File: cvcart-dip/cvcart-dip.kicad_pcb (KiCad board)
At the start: 2 copper layers, 6 parts, among them CON101 CV-EDGE, U101 W27C512

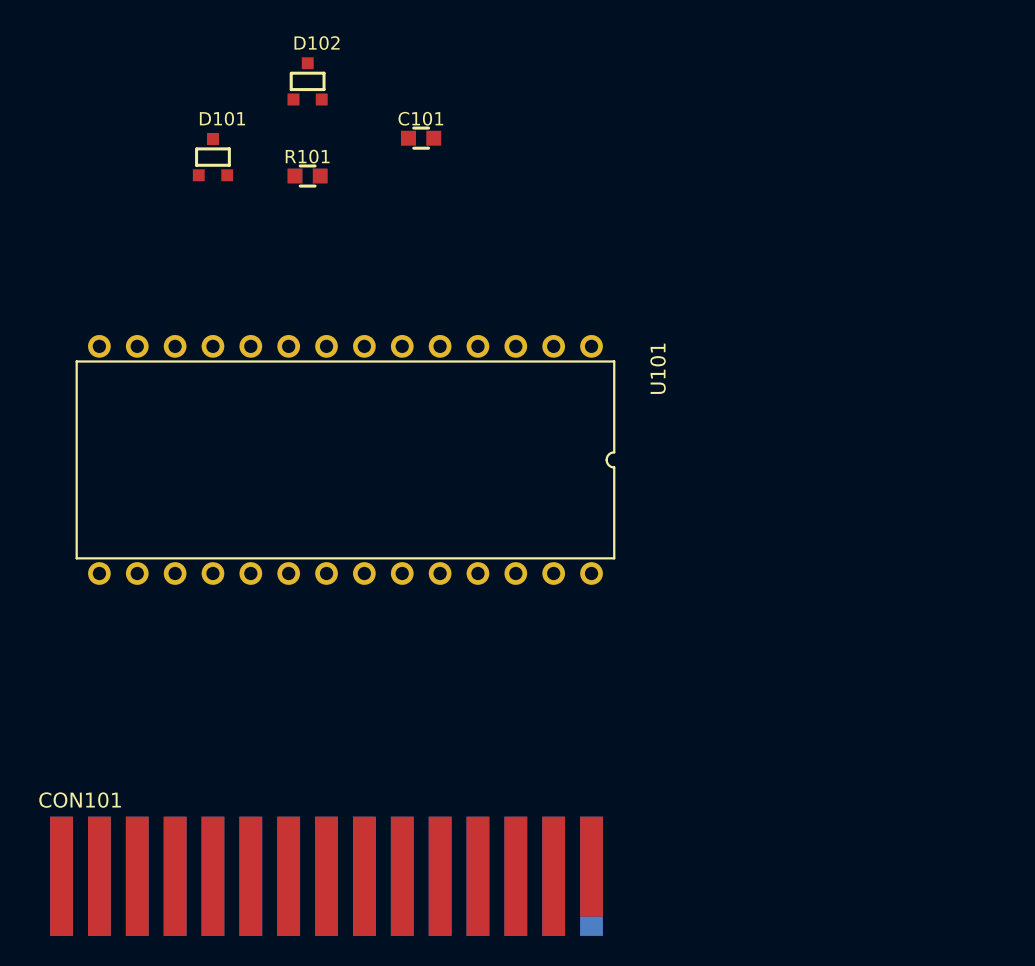
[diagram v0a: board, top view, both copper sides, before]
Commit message: routing traces
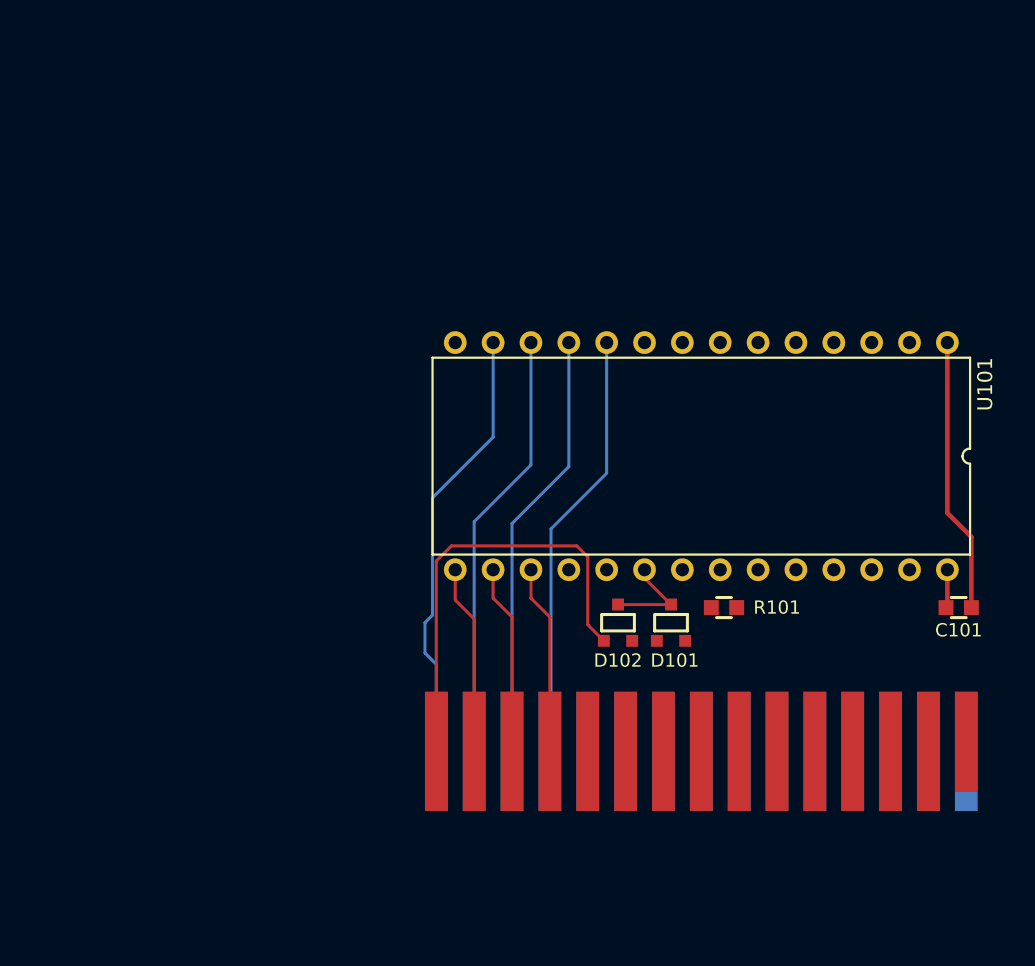
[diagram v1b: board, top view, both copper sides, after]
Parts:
- moved C101 47.9 mm to (166.9, 110.2)
- moved D101 43.8 mm to (147.6, 111.3)
- moved D102 41.9 mm to (144.0, 111.3)
- moved R101 40.2 mm to (151.1, 110.2), turned to 180 degrees
- moved CON101 26.5 mm to (131.8, 119.9)
- moved U101 23.9 mm to (166.1, 92.5)
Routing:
- net /~C000: track 0.00 -> 29.7 mm
- net /D2: track 0.00 -> 29.6 mm
- net /D0: track 0.00 -> 29.0 mm
- net /A0: track 0.00 -> 29.0 mm
- net /D1: track 0.00 -> 29.0 mm
- net GND: track 0.00 -> 18.4 mm
- net /D5: track 0.00 -> 12.7 mm
- net /D4: track 0.00 -> 12.7 mm
- net /D3: track 0.00 -> 12.7 mm
- net Net-(D101-Pad3): track 0.00 -> 6.63 mm
- net +5V: track 0.00 -> 2.58 mm
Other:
- net class Default: clearance 0.2 -> 0.1778; trace_width 0.25 -> 0.2032; via_dia 0.6 -> 0.6096; via_drill 0.4 -> 0.3048
- net class Power added: clearance 0.1778, trace_width 0.3048, via_dia 0.6096, via_drill 0.3048
- rule trace_clearance: 0.2 -> 0.1778
- rule trace_min: 0.2 -> 0.1778
- rule via_min_size: 0.4 -> 0.3048

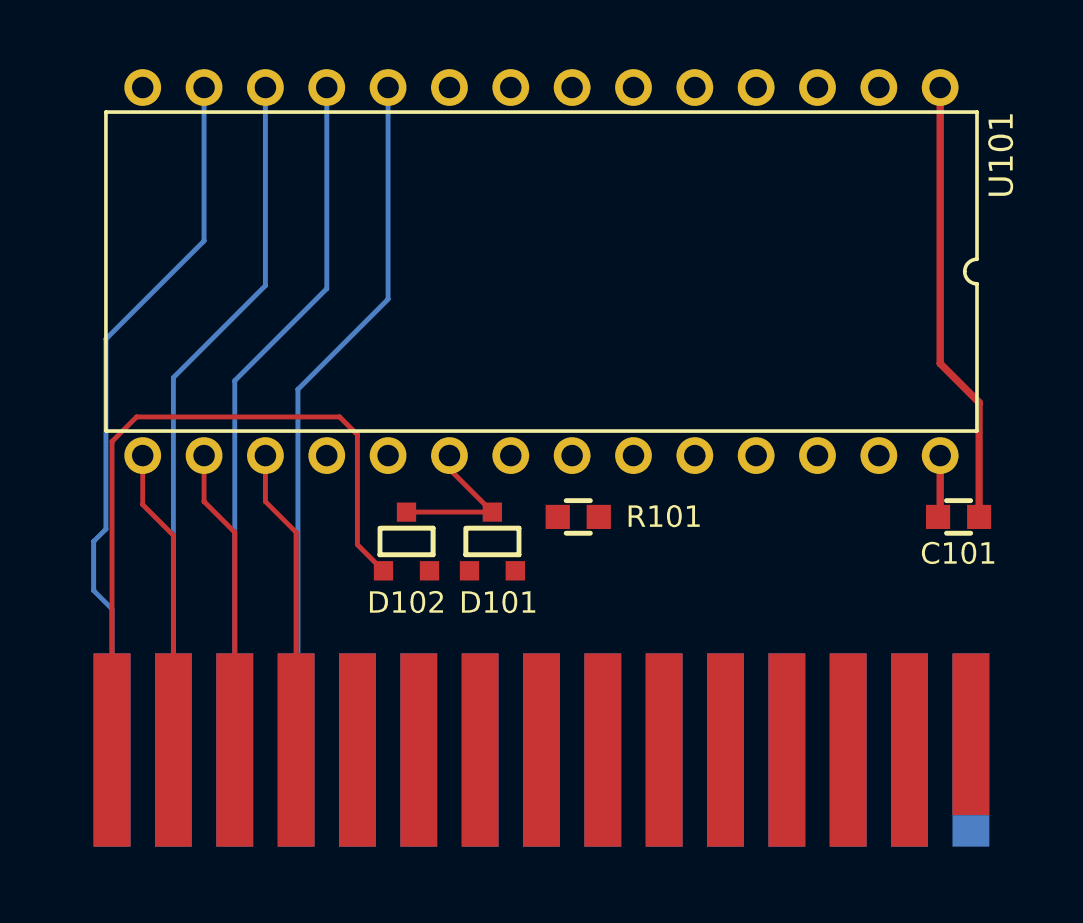
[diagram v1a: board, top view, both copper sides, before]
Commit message: layout work, missing ground plane
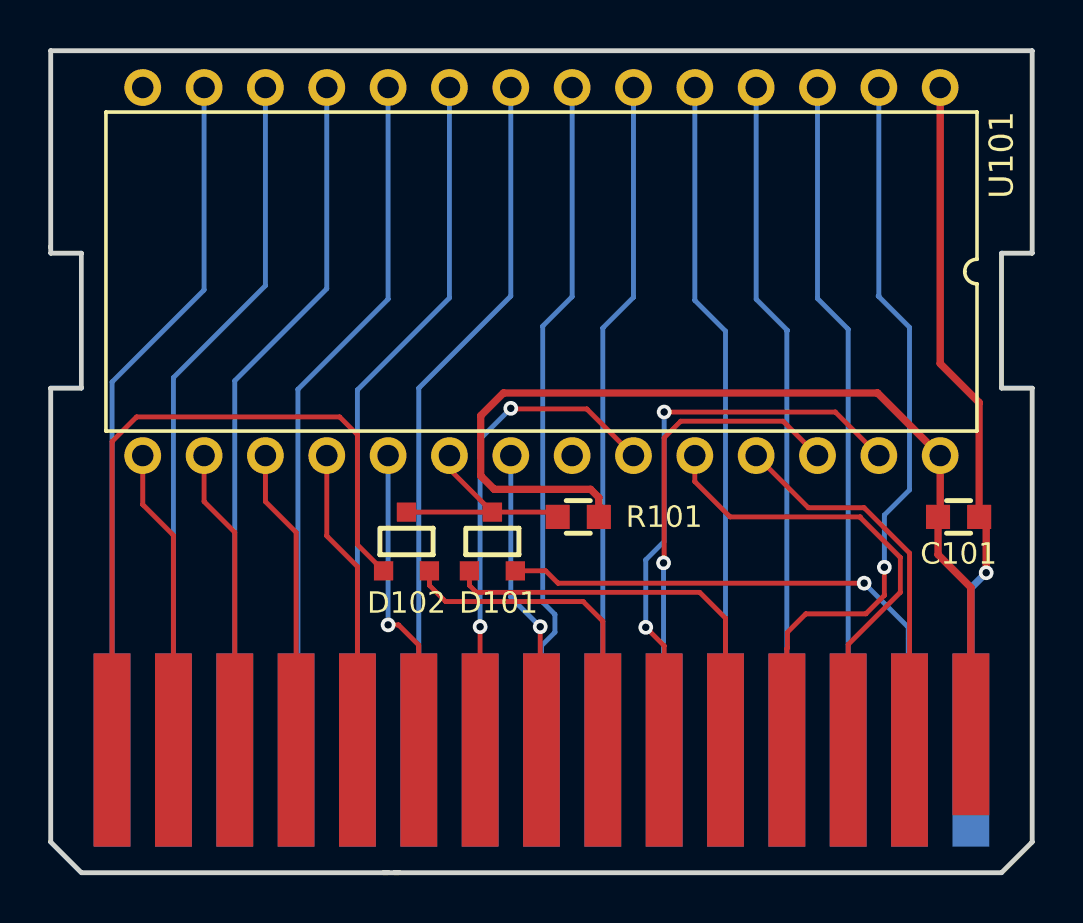
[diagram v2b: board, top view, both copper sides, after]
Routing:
- net +5V: track 2.58 -> 41.2 mm
- net /A12: track 0.00 -> 31.5 mm, vias 0 -> 1
- net /A2: track 0.00 -> 29.0 mm
- net /A1: track 0.00 -> 29.0 mm
- net /A3: track 0.00 -> 28.4 mm
- net /A6: track 0.00 -> 28.0 mm
- net /A7: track 0.00 -> 28.0 mm
- net /A5: track 0.00 -> 28.0 mm
- net /A4: track 0.00 -> 28.0 mm
- net /A14: track 0.00 -> 24.3 mm, vias 0 -> 2
- net /~E000: track 0.00 -> 22.3 mm, vias 0 -> 1
- net /A11: track 0.00 -> 21.3 mm, vias 0 -> 2
- net /A13: track 0.00 -> 20.2 mm, vias 0 -> 1
- net /A9: track 0.00 -> 19.8 mm
- net /~A000: track 0.00 -> 17.2 mm
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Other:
- board outline added: 40.6 x 34 mm

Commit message: added ground pours and keepouts
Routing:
- net GND: track 28.5 -> 33.1 mm, vias 1 -> 2
- added copper zone on B.Cu, net GND
- added copper zone on F.Cu, net GND
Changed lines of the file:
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@@
   (general
     (links 37)
-    (no_connects 23)
+    (no_connects 2)
     (area 115.086001 82.136 187.729715 125.068001)
     (thickness 1.6)
     (drawings 22)
-    (tracks 165)
+    (tracks 167)
     (zones 0)
     (modules 6)
@@
     (last_trace_width 0.2032)
     (trace_clearance 0.1778)
-    (zone_clearance 0.508)
-    (zone_45_only no)
+    (zone_clearance 0.381)
+    (zone_45_only yes)
     (trace_min 0.1778)
     (segment_width 0.2)
@@
       (outputformat 1)
       (mirror false)
-      (drillshape 1)
+      (drillshape 0)
       (scaleselection 1)
       (outputdirectory ""))
@@
       (effects (font (size 1 1) (thickness 0.15)))
     )
-    (fp_text value W27C512 (at 2.54 35.56 270) (layer F.Fab)
+    (fp_text value W27C512 (at 2.6162 -2.5908 270) (layer F.Fab)
       (effects (font (size 1 1) (thickness 0.15)))
     )
@@
   (segment (start 139.446 110.871) (end 139.446 119.888) (width 0.2032) (layer F.Cu) (net 2))
   (segment (start 138.176 109.601) (end 139.446 110.871) (width 0.2032) (layer F.Cu) (net 2))
+  (segment (start 150.876 107.696) (end 150.876 103.0732) (width 0.3048) (layer B.Cu) (net 3))
+  (via (at 150.876 103.0732) (size 0.6096) (drill 0.3048) (layers F.Cu B.Cu) (net 3))
   (segment (start 168.021 112.5474) (end 168.021 110.529) (width 0.3048) (layer F.Cu) (net 3))
   (segment (start 168.021 110.529) (end 167.728 110.236) (width 0.3048) (layer F.Cu) (net 3))
@@
   (segment (start 145.796 108.258) (end 147.574 110.036) (width 0.2032) (layer F.Cu) (net 31))
   (segment (start 144.018 110.036) (end 147.574 110.036) (width 0.2032) (layer F.Cu) (net 31) (status 10))
+  (zone (net 0) (net_name "") (layer F.Cu) (hatch full 0.508)
+    (connect_pads (clearance 0.508))
+    (min_thickness 0.254)
+    (keepout (tracks allowed) (vias allowed) (copperpour not_allowed))
+    (fill (arc_segments 16) (thermal_gap 0.508) (thermal_bridge_width 0.508))
+    (polygon
+      (pts
+        (xy 129.286 115.57) (xy 129.286 124.968) (xy 169.9514 124.968) (xy 169.926 115.57)
+      )
+    )
+  )
+  (zone (net 3) (net_name GND) (layer F.Cu) (hatch full 0.508)
+    (connect_pads (clearance 0.381))
+    (min_thickness 0.2032)
+    (fill yes (arc_segments 16) (thermal_gap 0.3048) (thermal_bridge_width 0.254))
+    (polygon
+      (pts
+        (xy 129.286 90.932) (xy 129.286 124.968) (xy 169.926 124.968) (xy 169.926 90.932)
+      )
+    )
+  )
+  (zone (net 3) (net_name GND) (layer B.Cu) (hatch full 0.508)
+    (connect_pads (clearance 0.381))
+    (min_thickness 0.2032)
+    (fill yes (arc_segments 16) (thermal_gap 0.3048) (thermal_bridge_width 0.254))
+    (polygon
+      (pts
+        (xy 129.286 90.932) (xy 129.286 124.968) (xy 169.926 124.968) (xy 169.9006 90.932)
+      )
+    )
+  )
+  (zone (net 0) (net_name "") (layer B.Cu) (hatch full 0.508)
+    (connect_pads (clearance 0.508))
+    (min_thickness 0.254)
+    (keepout (tracks allowed) (vias allowed) (copperpour not_allowed))
+    (fill (arc_segments 16) (thermal_gap 0.508) (thermal_bridge_width 0.508))
+    (polygon
+      (pts
+        (xy 129.286 115.57) (xy 129.286 124.968) (xy 169.926 124.968) (xy 169.926 115.57)
+      )
+    )
+  )
 )

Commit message: fully licensed as CERN OHL v.1.2
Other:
- board text added: "cvcart-dip_1.0 René Richard Licensed under CERN OHL v.1.2 https://github.com/db-electronics/cvcarts-kicad"
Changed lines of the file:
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@@
-(kicad_pcb (version 4) (host pcbnew 4.0.5-e0-6337~49~ubuntu16.04.1)
+(kicad_pcb (version 4) (host pcbnew 4.0.7-e2-6376~58~ubuntu16.04.1)
   (general
     (links 37)
-    (no_connects 2)
+    (no_connects 0)
     (area 115.086001 82.136 187.729715 125.068001)
     (thickness 1.6)
-    (drawings 22)
+    (drawings 23)
     (tracks 167)
     (zones 0)
@@
   )
   (page A4)
+  (title_block
+    (title "Colecovision DIP Cartridge")
+    (date 2017-10-16)
+    (rev 1.0)
+    (company "db Electronics")
+    (comment 1 "copyright: René Richard")
+    (comment 2 https://github.com/db-electronics/cvcarts-kicad)
+    (comment 3 http://ohwr.org/cernohl)
+    (comment 4 "Licensed under CERN OHL v.1.2”")
+  )
   (layers
     (0 F.Cu signal)
@@
     (descr SOT23)
     (attr smd)
-    (fp_text reference D101 (at 0.254 2.54) (layer F.SilkS)
+    (fp_text reference D101 (at 3.7084 1.016) (layer F.SilkS)
       (effects (font (size 0.889 0.889) (thickness 0.2032)))
     )
@@
     (descr SOT23)
     (attr smd)
-    (fp_text reference D102 (at 0 2.54) (layer F.SilkS)
+    (fp_text reference D102 (at -2.667 -1.2954) (layer F.SilkS)
       (effects (font (size 0.889 0.889) (thickness 0.2032)))
     )
@@
     )
   )
+  (gr_text "cvcart-dip_1.0\nRené Richard\nLicensed under CERN OHL v.1.2\nhttps://github.com/db-electronics/cvcarts-kicad" (at 167.005 98.3742) (layer B.SilkS)
+    (effects (font (size 0.889 0.889) (thickness 0.2032)) (justify left mirror))
+  )
   (gr_line (start 143.0782 124.968) (end 143.7132 124.968) (angle 90) (layer Edge.Cuts) (width 0.2))
